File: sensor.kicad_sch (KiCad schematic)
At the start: 17 parts, among them U4 ST_SENSOR_2, U5 IIS3DHHCTR

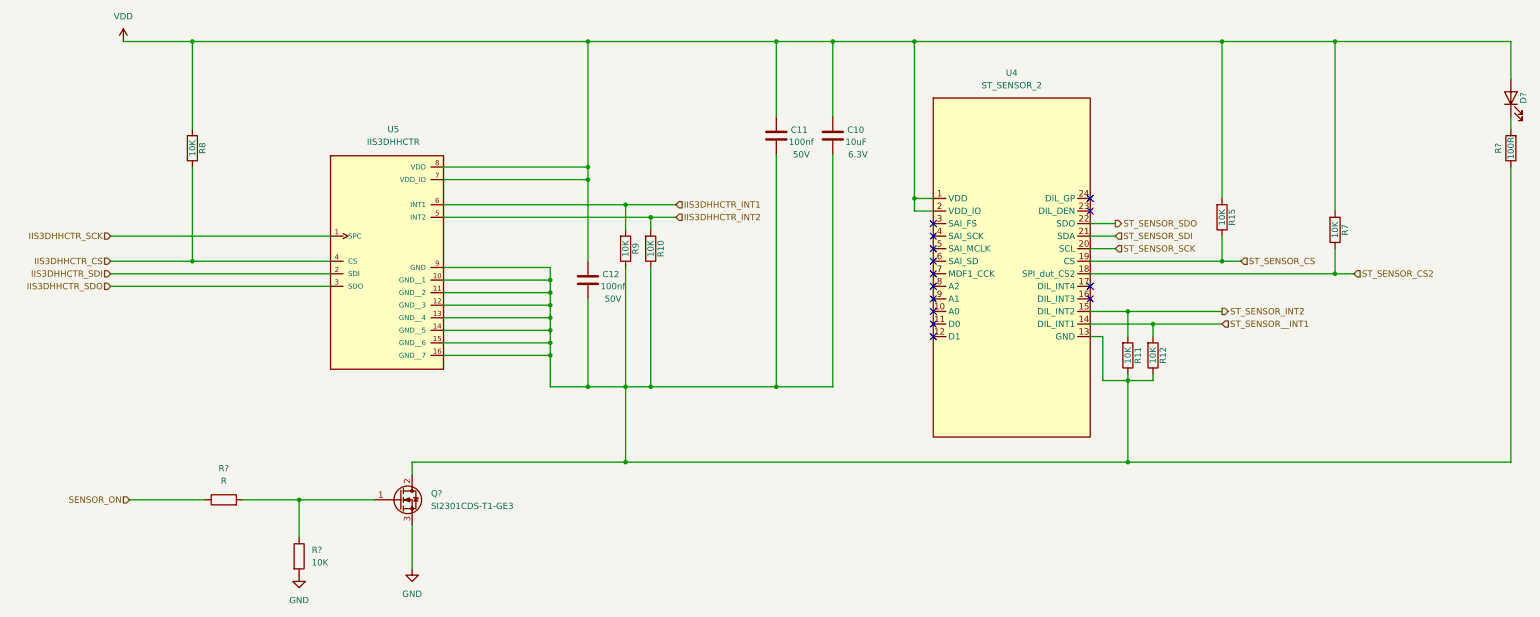
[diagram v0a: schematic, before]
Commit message: change power add buzzer
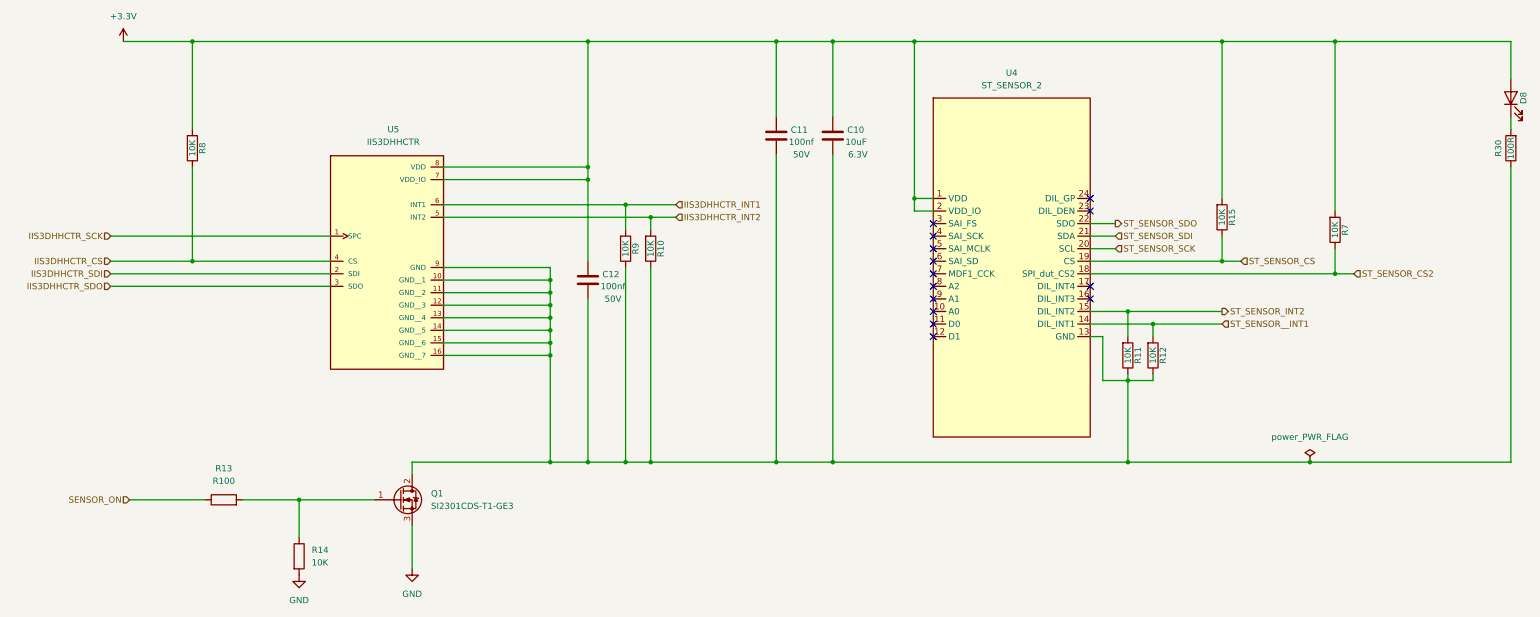
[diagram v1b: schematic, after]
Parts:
- R13: renamed from R?; value R -> R100; footprint (none) -> Resistor_SMD:R_0603_1608Metric
- gave numbers to parts that had none: 4
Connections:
- net VDD renamed +3.3V

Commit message: remove hellen
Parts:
- removed R14: 10K, symbol Device:R
- added R2: 10K, Resistor_SMD:R_0603_1608Metric, symbol Device:R
- U5: footprint IIS3DHHCTR:IC_IIS3DHHCTR -> dnt:CCLGA-16L_5X5X1P7_STM
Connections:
- net GND: now also R2.1
- net at Q1.1 (G), R13.2: now also R2.2
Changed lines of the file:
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@@
+	(symbol
+		(lib_id "Device:R")
+		(at 73.66 128.27 0)
+		(mirror x)
+		(unit 1)
+		(exclude_from_sim no)
+		(in_bom yes)
+		(on_board yes)
+		(dnp no)
+		(property "Reference" "R2"
+			(at 75.692 128.27 90)
+			(effects
+				(font
+					(size 1.27 1.27)
+				)
+			)
+		)
+		(property "Value" "10K"
+			(at 73.66 128.27 90)
+			(effects
+				(font
+					(size 1.27 1.27)
+				)
+			)
+		)
+		(property "Footprint" "Resistor_SMD:R_0603_1608Metric"
+			(at 132.842 186.69 90)
+			(effects
+				(font
+					(size 1.524 1.524)
+				)
+				(hide yes)
+			)
+		)
+		(property "Datasheet" "~"
+			(at 222.25 187.325 0)
+			(effects
+				(font
+					(size 1.524 1.524)
+				)
+				(hide yes)
+			)
+		)
+		(property "Description" "Resistor"
+			(at 73.66 128.27 0)
+			(effects
+				(font
+					(size 1.27 1.27)
+				)
+				(hide yes)
+			)
+		)
+		(property "Part #" "RMCF0603JT10K0"
+			(at -29.21 30.48 0)
+			(effects
+				(font
+					(size 1.27 1.27)
+				)
+				(hide yes)
+			)
+		)
+		(property "VEND" "DIGI"
+			(at -29.21 30.48 0)
+			(effects
+				(font
+					(size 1.27 1.27)
+				)
+				(hide yes)
+			)
+		)
+		(property "VEND#" "RMCF0603JT10K0CT-ND"
+			(at -29.21 30.48 0)
+			(effects
+				(font
+					(size 1.27 1.27)
+				)
+				(hide yes)
+			)
+		)
+		(property "Manufacturer" "StackPole"
+			(at -29.21 30.48 0)
+			(effects
+				(font
+					(size 1.27 1.27)
+				)
+				(hide yes)
+			)
+		)
+		(property "LCSC" "C25804"
+			(at 73.66 128.27 0)
+			(effects
+				(font
+					(size 1.27 1.27)
+				)
+				(hide yes)
+			)
+		)
+		(pin "1"
+		)
+		(pin "2"
+		)
+		(instances
+			(project "l8-kicad"
+				(path "/8d063f79-9282-4820-bcf4-1ff3c006cf08/801ffdec-7184-42a0-bbdb-64e97598ca97"
+					(reference "R2")
+					(unit 1)
+				)
+			)
+		)
+	)
 	(symbol
 		(lib_id "Device:R")
@@
 	)
 	(symbol
-		(lib_id "Device:R")
-		(at 73.66 128.27 0)
-		(unit 1)
-		(exclude_from_sim no)
-		(in_bom yes)
-		(on_board yes)
-		(dnp no)
-		(fields_autoplaced yes)
-		(property "Reference" "R14"
-			(at 76.2 126.9999 0)
-			(effects
-				(font
-					(size 1.27 1.27)
-				)
-				(justify left)
-			)
-		)
-		(property "Value" "10K"
-			(at 76.2 129.5399 0)
-			(effects
-				(font
-					(size 1.27 1.27)
-				)
-				(justify left)
-			)
-		)
-		(property "Footprint" ""
-			(at 71.882 128.27 90)
-			(effects
-				(font
-					(size 1.27 1.27)
-				)
-				(hide yes)
-			)
-		)
-		(property "Datasheet" "~"
-			(at 73.66 128.27 0)
-			(effects
-				(font
-					(size 1.27 1.27)
-				)
-				(hide yes)
-			)
-		)
-		(property "Description" "Resistor"
-			(at 73.66 128.27 0)
-			(effects
-				(font
-					(size 1.27 1.27)
-				)
-				(hide yes)
-			)
-		)
-		(pin "1"
-		)
-		(pin "2"
-		)
-		(instances
-			(project ""
-				(path "/8d063f79-9282-4820-bcf4-1ff3c006cf08/801ffdec-7184-42a0-bbdb-64e97598ca97"
-					(reference "R14")
-					(unit 1)
-				)
-			)
-		)
-	)
-	(symbol
 		(lib_id "l8-kicad-rescue:GND-power")
 		(at 73.66 132.08 0)
@@
 			)
 		)
-		(property "Footprint" "IIS3DHHCTR:IC_IIS3DHHCTR"
+		(property "Footprint" "dnt:CCLGA-16L_5X5X1P7_STM"
 			(at 92.71 59.69 0)
 			(effects

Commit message: pre quilter
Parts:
- added TP3, TP4: IIS3DHHCTR_SDI, TestPoint:TestPoint_Pad_D2.0mm, symbol Connector:TestPoint
- added TP5: IIS3DHHCTR_SCK, TestPoint:TestPoint_Pad_D2.0mm, symbol Connector:TestPoint
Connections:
- net IIS3DHHCTR_SCK: now also TP5.1
- net IIS3DHHCTR_SDI: now also TP4.1
- net IIS3DHHCTR_SDO: now also TP3.1

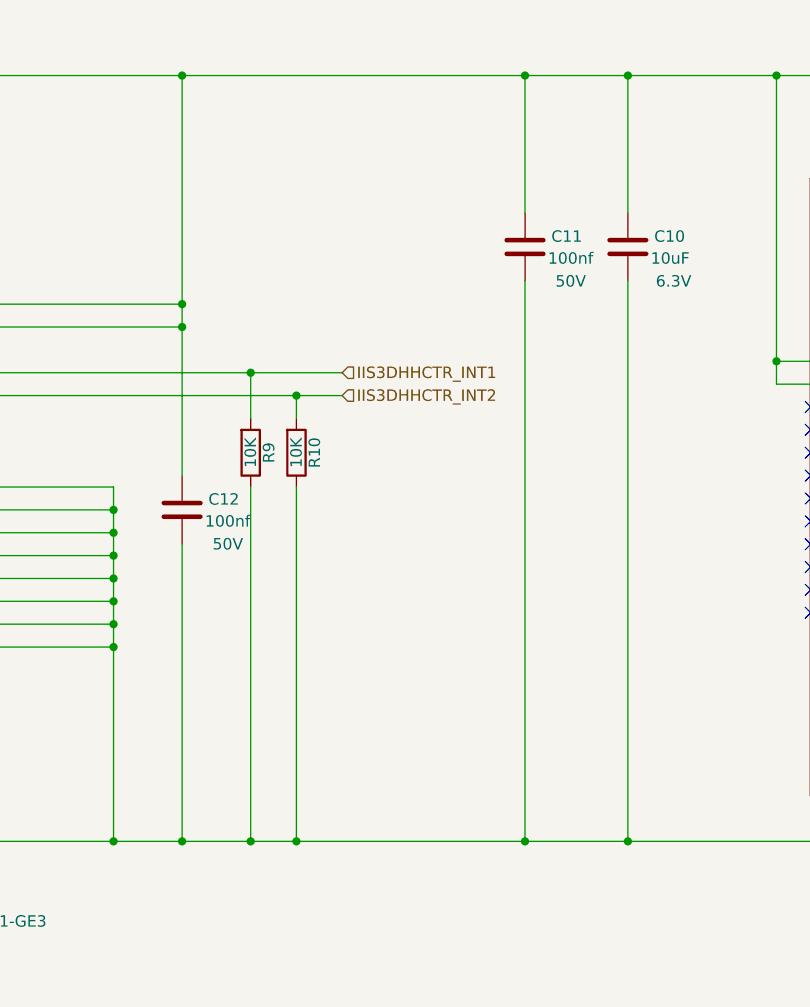
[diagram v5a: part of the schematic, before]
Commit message: changed to tp and subbed to quilter
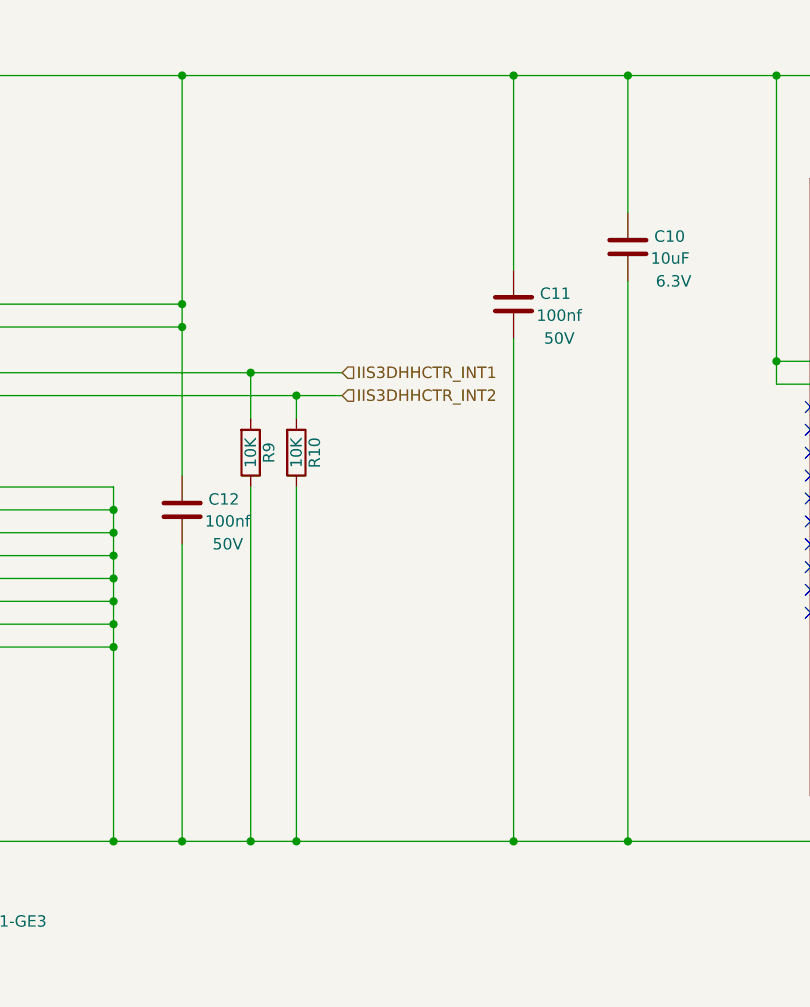
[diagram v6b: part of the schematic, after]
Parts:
- C10: now in the parts list
- TP3, TP4, TP5: footprint TestPoint:TestPoint_Pad_D2.0mm -> TestPoint:TestPoint_Pad_D1.0mm
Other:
- moved on the sheet: C11

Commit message: pre quilter - actually saved
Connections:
- no-connect marks 14 -> 2
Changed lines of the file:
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@@
-	)
-	(no_connect
-		(at 201.93 66.04)
-	)
-	(no_connect
-		(at 201.93 60.96)
-	)
-	(no_connect
-		(at 201.93 78.74)
-	)
-	(no_connect
-		(at 201.93 73.66)
-	)
-	(no_connect
-		(at 233.68 55.88)
 	)
 	(no_connect
 		(at 233.68 73.66)
-	)
-	(no_connect
-		(at 201.93 83.82)
-	)
-	(no_connect
-		(at 201.93 63.5)
-	)
-	(no_connect
-		(at 233.68 58.42)
-	)
-	(no_connect
-		(at 201.93 71.12)
-	)
-	(no_connect
-		(at 201.93 81.28)
-	)
-	(no_connect
-		(at 201.93 76.2)
-	)
-	(no_connect
-		(at 201.93 68.58)
 	)
 	(wire
@@
 			)
 		)
-		(property "Description" "20V 3.1A 112mΩ@4.5V,2.8A 1V@250uA 1PCSPChannel SOT-23 MOSFETs ROHS"
+		(property "Description" "Generic N-Channel Power MOSFET"
 			(at 93.98 116.84 0)
 			(effects

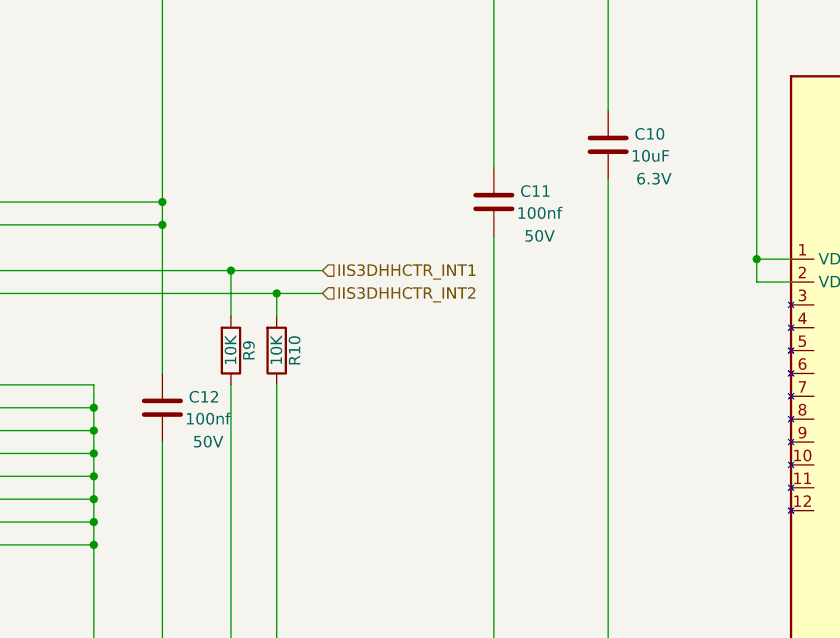
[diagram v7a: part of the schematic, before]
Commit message: smaller caps remove ringing resistors
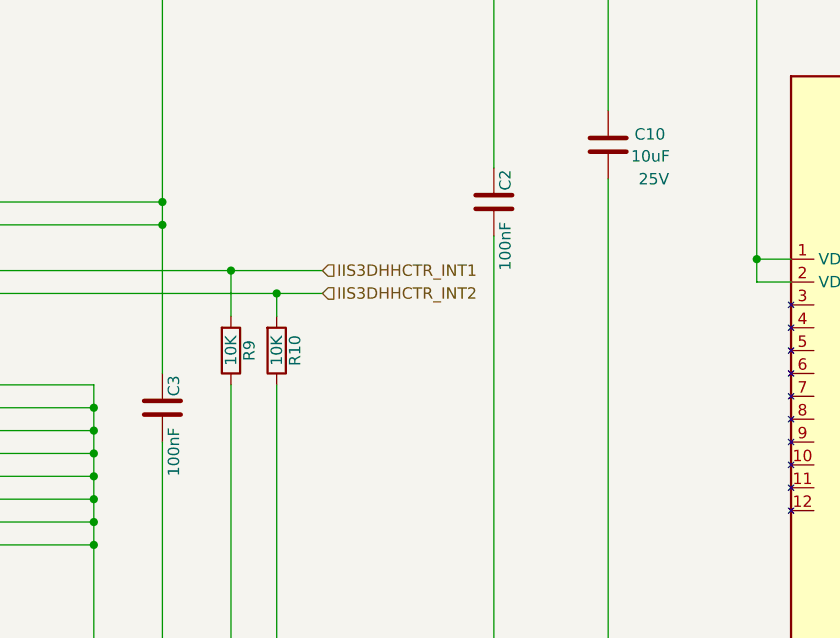
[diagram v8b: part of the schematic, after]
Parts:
- removed C11, C12: 100nf, Capacitor_SMD:C_0201_0603Metric, symbol Device:C
- added C2, C3: 100nF, Capacitor_SMD:C_01005_0402Metric, symbol Device:C
- C10: LCSC (none) -> C96446; Voltage 6.3V -> 25V
- R11, R12, R15, R7, R8: Manufacturer StackPole -> (none); Part # RMCF0603JT10K0 -> (none); VEND DIGI -> (none); VEND# RMCF0603JT10K0CT-ND -> (none)
- R30: LCSC C21190 -> C22775; Manufacturer StackPole -> (none); Part # RMCF0603JJ1K00 -> (none); VEND DIGI -> (none); VEND# RMCF0603JJ1K00CT-ND -> (none)
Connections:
- net +3.3V: now also C2.1, C3.1
- net at C10.2, Q1.2 (D), R10.1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: now also C2.2, C3.2
